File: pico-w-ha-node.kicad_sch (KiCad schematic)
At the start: 31 parts, among them J1 USB_C_Receptacle_PowerOnly_6P, J2 Conn_01x04, J3 Conn_01x04, Q1 STD18NF03L, Q10 si2369, Q2 STD18NF03L, Q6 str2n2vh5, Q7 si2369, Q8 si2369, Q9 str2n2vh5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

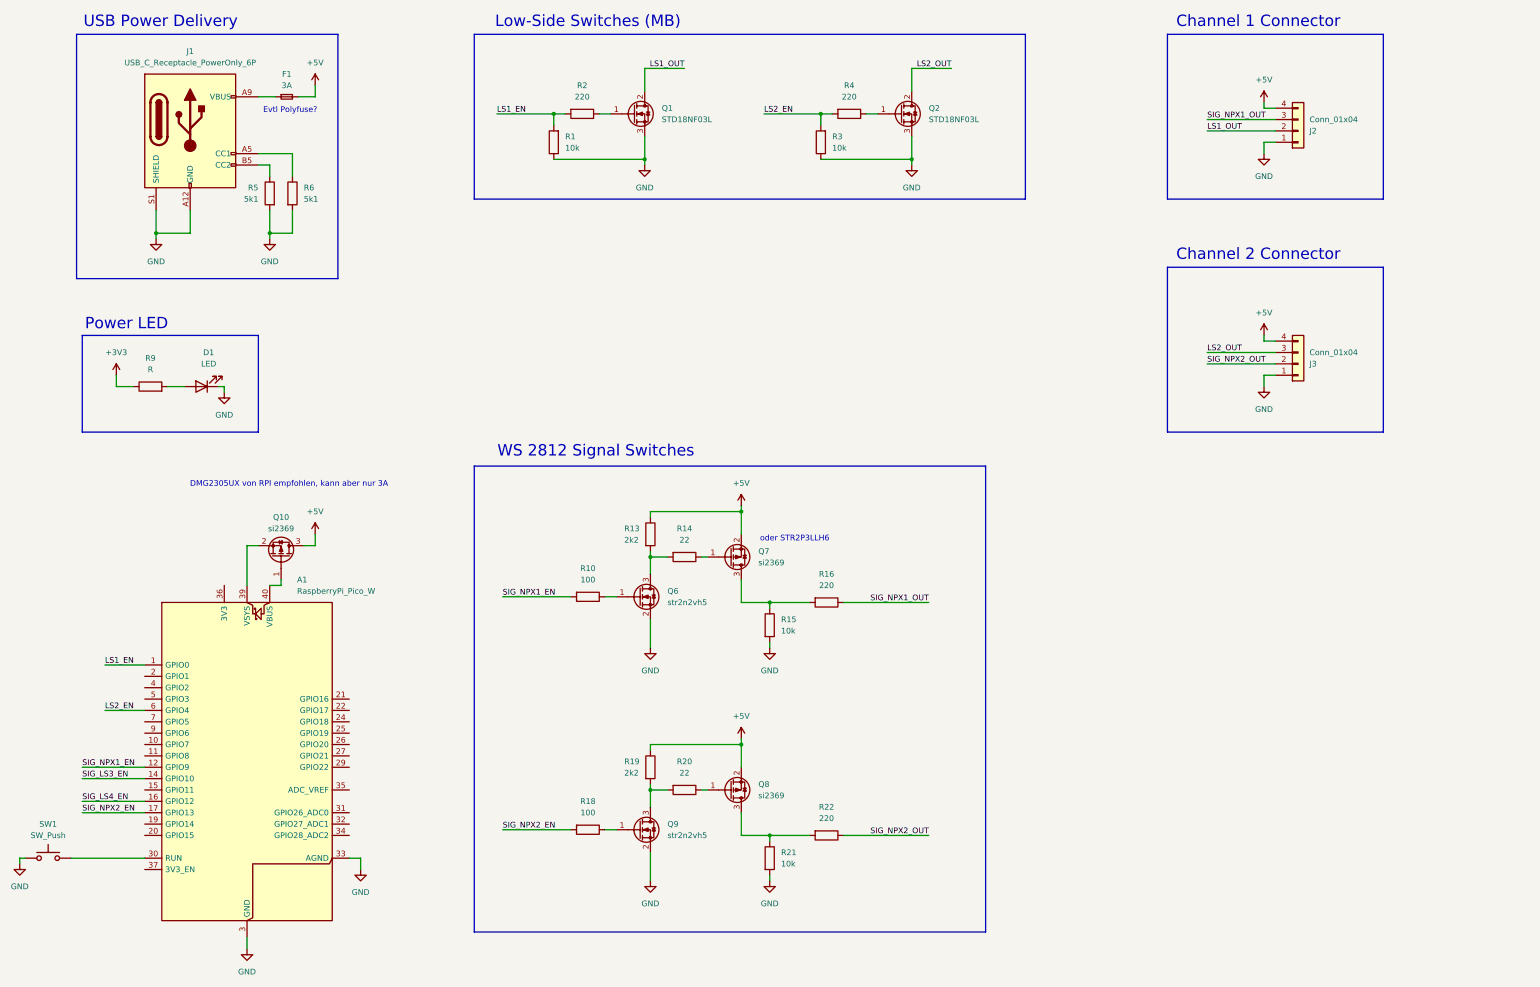
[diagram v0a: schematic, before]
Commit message: Changes NPX signal circuit, adds some capacitors, temperature sensor and alternative power input
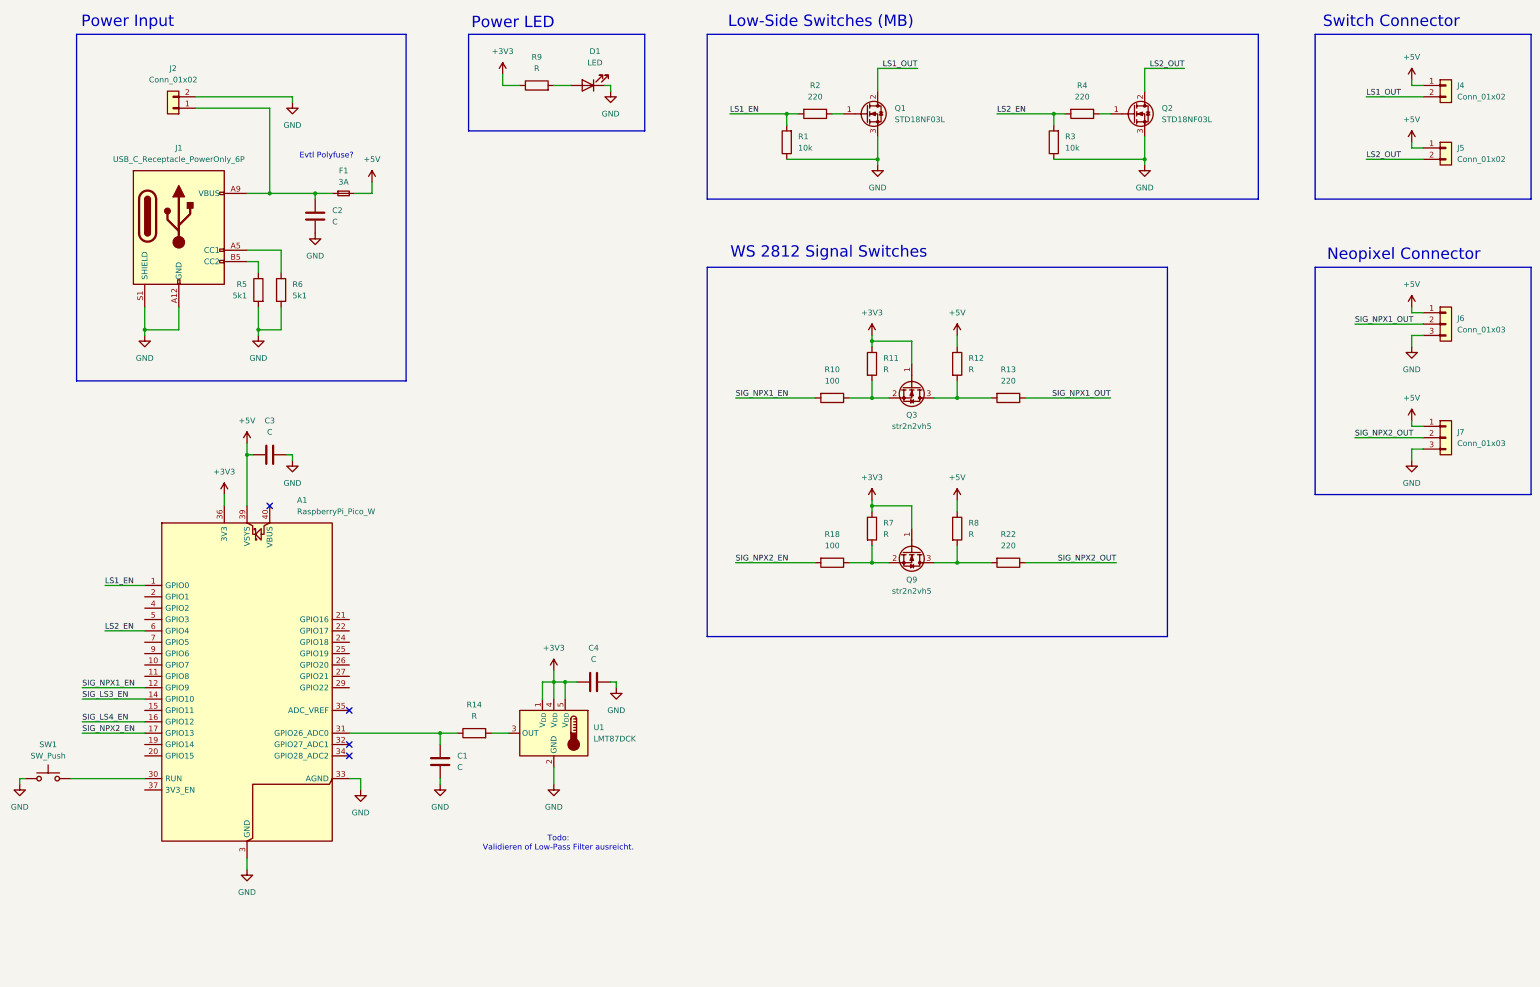
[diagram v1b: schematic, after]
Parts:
- removed J2, J3: Conn_01x04, FSTW_footprints:WE_WR-TBL_Serie_3221_3.5mm_691322110005, symbol Connector_Generic:Conn_01x04
- removed Q10, Q7, Q8: si2369, Package_TO_SOT_SMD:SOT-23, symbol Transistor_FET:Q_PMOS_GSD
- removed Q6: str2n2vh5, Package_TO_SOT_SMD:SOT-23, symbol Transistor_FET:Q_NMOS_GSD
- removed R15, R21: 10k, Resistor_SMD:R_0603_1608Metric_Pad0.98x0.95mm_HandSolder, symbol Device:R
- removed R16: 220, Resistor_SMD:R_0603_1608Metric_Pad0.98x0.95mm_HandSolder, symbol Device:R
- removed R19: 2k2, Resistor_SMD:R_0603_1608Metric_Pad0.98x0.95mm_HandSolder, symbol Device:R
- removed R20: 22, Resistor_SMD:R_0603_1608Metric_Pad0.98x0.95mm_HandSolder, symbol Device:R
- added C1, C4: C, Capacitor_SMD:C_0603_1608Metric_Pad1.08x0.95mm_HandSolder, symbol Device:C
- added C2, C3: C, symbol Device:C
- added J2, J4, J5: Conn_01x02, Connector_Molex:Molex_CLIK-Mate_502585-0270_1x02-1MP_P1.50mm_Horizontal, symbol Connector_Generic:Conn_01x02
- added J6, J7: Conn_01x03, Connector_Molex:Molex_CLIK-Mate_502585-0370_1x03-1MP_P1.50mm_Horizontal, symbol Connector_Generic:Conn_01x03
- added Q3: str2n2vh5, Package_TO_SOT_SMD:SOT-23, symbol Transistor_FET:Q_NMOS_GSD
- added R11, R12, R7, R8: R, Resistor_SMD:R_0603_1608Metric_Pad0.98x0.95mm_HandSolder, symbol Device:R
- added U1: LMT87DCK, Package_TO_SOT_SMD:SOT-353_SC-70-5, symbol Sensor_Temperature:LMT87DCK
- A1: footprint RaspberryPi_Pico:RaspberryPi_Pico_W_SMD_HandSolder -> Module:RaspberryPi_Pico_W_SMD
- R13: value 2k2 -> 220
- R14: value 22 -> R
- R5, R6: footprint (none) -> Resistor_SMD:R_0603_1608Metric_Pad0.98x0.95mm_HandSolder
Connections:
- net +3V3: now also A1.36 (3V3), Q9.1 (G), C4.1, Q3.1 (G), R11.1, R7.1, U1.1 (V_{DD}), U1.4 (V_{DD}), U1.5 (V_{DD})
- net +5V: now also A1.39 (VSYS), C3.1, J4.1 (Pin_1), J5.1 (Pin_1), J6.1 (Pin_1), J7.1 (Pin_1), R12.1, R8.1; no longer R13.1
- net GND: now also C1.2, C2.2, C3.2, C4.2, J2.2 (Pin_2), J6.3 (Pin_3), J7.3 (Pin_3), U1.2 (GND); no longer Q9.2 (S)
- net LS1_OUT: now also J4.2 (Pin_2)
- net LS2_OUT: now also J5.2 (Pin_2)
- net SIG_NPX1_OUT: now also R13.1, J6.2 (Pin_2)
- net SIG_NPX2_OUT: now also J7.2 (Pin_2)
- net at R22.2: now also Q9.3 (D), R8.2
- net at R13.2: now also Q3.3 (D), R12.2; no longer R14.2
- net at A1.31 (GPIO26_ADC0): now also R14.1, C1.1
- net at F1.1, J1.A9 (VBUS), J1.B9 (VBUS): now also C2.1, J2.1 (Pin_1)
- net at R18.1: now also Q9.2 (S), R7.2; no longer Q9.1 (G)
- net at R10.1: now also Q3.2 (S), R11.2
- new net: R14.2, U1.3 (OUT)
- no-connect marks 0 -> 4
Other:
- note added: "Neopixel Connector"
- note added: "Power Input"
- note added: "Switch Connector"
- note added: "Todo: Validieren of Low-Pass Filter ausreicht."
- note removed: "Channel 1 Connector"
- note removed: "Channel 2 Connector"
- note removed: "DMG2305UX von RPI empfohlen, kann aber nur 3A"
- note removed: "USB Power Delivery"
- note removed: "oder STR2P3LLH6"
- moved on the sheet: A1, D1, F1, J1, Q1, Q2, Q9, R1, R18, R2, R22, R3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

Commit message: Adds 3rd output via USB-A and some additional capacitors.
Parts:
- removed C2: C, symbol Device:C
- removed Q1, Q2: STD18NF03L, Package_TO_SOT_SMD:TO-252-2, symbol Transistor_FET:Q_NMOS_GDS
- removed SW1: SW_Push, Button_Switch_SMD:SW_SPST_TL3305A, symbol Switch:SW_Push
- added C2, C5, C9: 820µ, Capacitor_THT:CP_Radial_D10.0mm_P5.00mm, symbol Device:C_Polarized
- added C6, C7, C8: 100n, Capacitor_SMD:C_0805_2012Metric, symbol Device:C
- added J8: USB_A, symbol Connector:USB_A
- added Q1, Q2, Q4: str2n2vh5, Package_TO_SOT_SMD:SOT-23, symbol Transistor_FET:Q_NMOS_GSD
- added R15: 10k, Resistor_SMD:R_0603_1608Metric_Pad0.98x0.95mm_HandSolder, symbol Device:R
- added R16: 220, Resistor_SMD:R_0603_1608Metric_Pad0.98x0.95mm_HandSolder, symbol Device:R
- C3: footprint (none) -> Capacitor_THT:CP_Radial_D10.0mm_P5.00mm; symbol Device:C -> Device:C_Polarized
- C4: value C -> 100n
- F1: footprint Fuse:Fuse_0603_1608Metric_Pad1.05x0.95mm_HandSolder -> Fuse:Fuse_1206_3216Metric
- J2: footprint Connector_Molex:Molex_CLIK-Mate_502585-0270_1x02-1MP_P1.50mm_Horizontal -> Connector_Molex:Molex_Micro-Fit_3.0_43650-0212_1x02-1MP_P3.00mm_Horizontal
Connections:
- net +5V: now also C2.1, C5.1, C6.1, C7.1, C8.1, C9.1, J8.1 (VBUS)
- net GND: now also C2.2, C5.2, C6.2, C7.2, C8.2, C9.2, J8.5 (Shield), Q1.2 (S), Q2.2 (S), Q4.2 (S), R15.1
- net LS1_OUT: now also Q4.3 (D)
- net LS2_OUT: now also Q1.3 (D)
- net at R2.1: now also Q4.1 (G)
- net at R4.1: now also Q1.1 (G)
- new net: Q2.1 (G), R16.1
- new net LS3_EN: R15.2, R16.2
- new net LS3_OUT: J8.4 (GND), Q2.3 (D)
- no-connect marks 4 -> 6
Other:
- note added: "Todo: Validieren ob Low-Pass Filter ausreicht."
- note removed: "Todo: Validieren of Low-Pass Filter ausreicht."
- moved on the sheet: D1, J6, J7, Q3, Q9, R1, R10, R11, R12, R13, R18, R2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
